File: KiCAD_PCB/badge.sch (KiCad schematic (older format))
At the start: 78 parts, among them Q1 BC847, Q2 BC847, Q3 BC847, U1 switch, U2 LM1117-3.3, U3 button, U4 digijoy, U5 button, U6 wrover, U7 2jumpers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

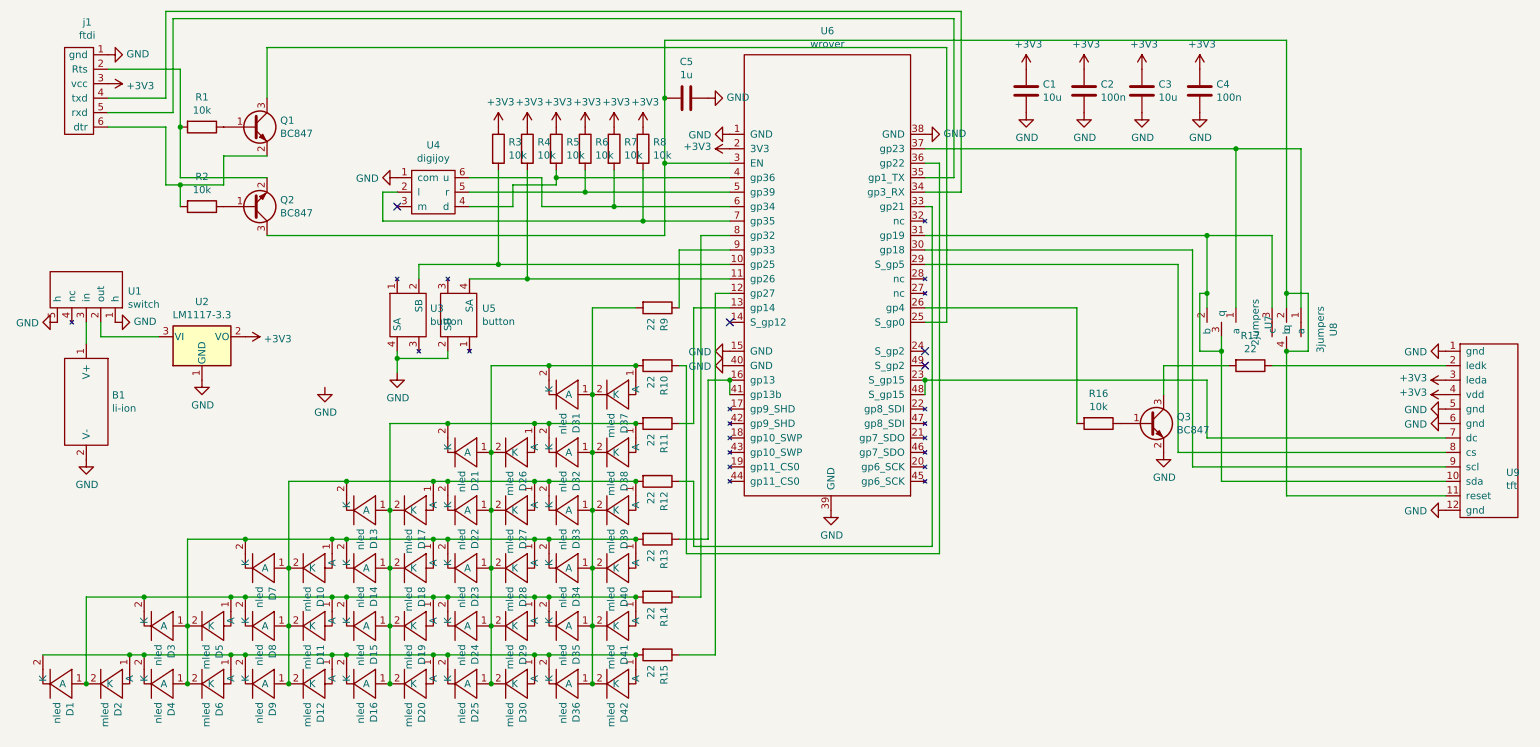
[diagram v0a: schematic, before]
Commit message: deleted two-transistor helper circuit on gp0/reset that was causing trouble when not connected to an ftdi module same circuit now included in programmer
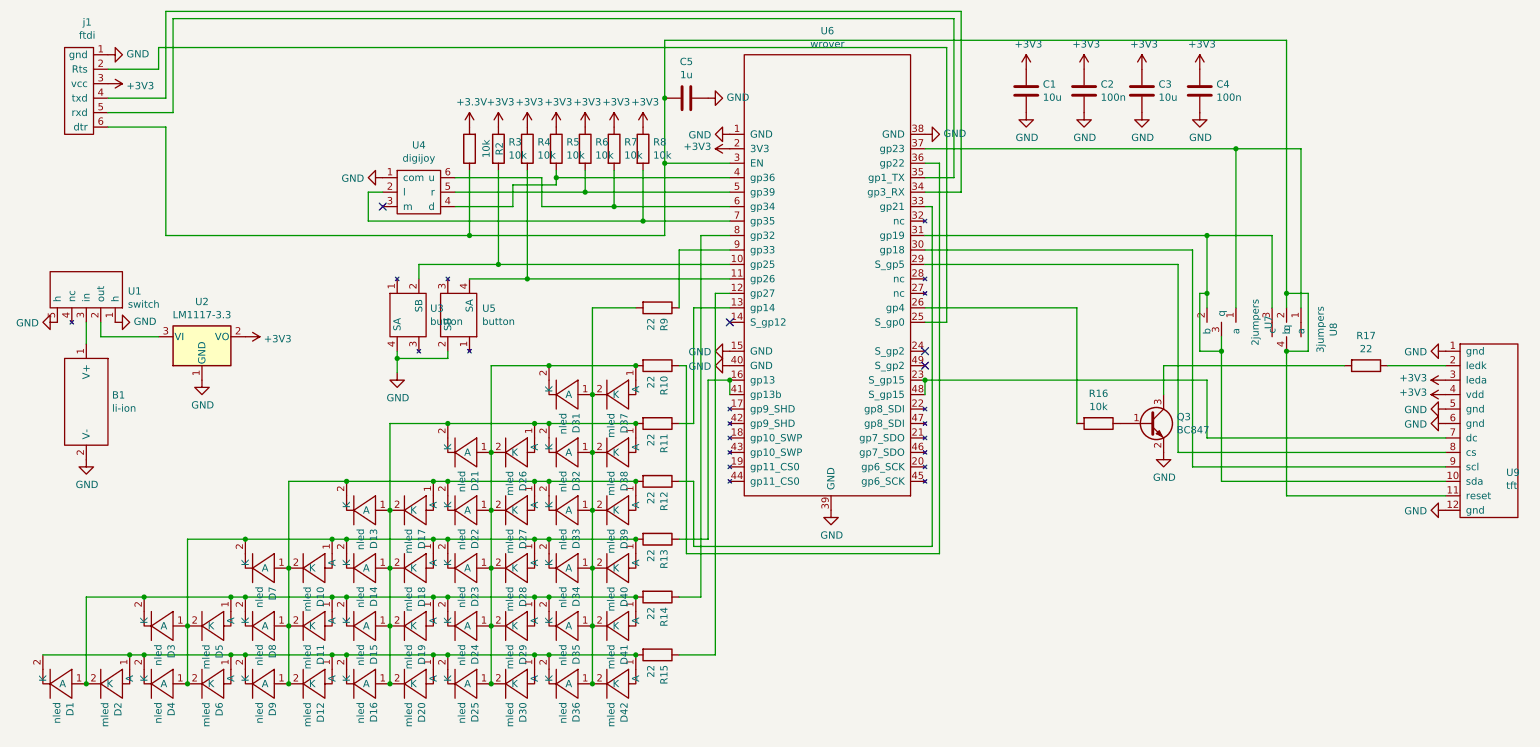
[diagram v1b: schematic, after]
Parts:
- removed Q1, Q2: BC847, Package_TO_SOT_SMD:SOT-23, symbol Transistor_BJT:BC847
- removed R1: 10k, LED_SMD:LED_1206_3216Metric_Pad1.42x1.75mm_HandSolder, symbol Device:R
- U8: footprint badge:2jumpers -> badge:3jumpers
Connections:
- net +3V3: now also R2.2
- net at U6.25 (S_gp0): now also j1.2 (Rts)
- net at C5.2, U6.3 (EN), U8.2 (b)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: now also R2.1, j1.6 (dtr)
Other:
- moved on the sheet: R17, R2, U4
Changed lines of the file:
@@
 EESchema Schematic File Version 4
-LIBS:badge-cache
 EELAYER 26 0
 EELAYER END
@@
 L badge:digijoy U4
 U 1 1 5F04E97E
-P 3300 4000
-F 0 "U4" H 3300 4325 50  0000 C CNN
-F 1 "digijoy" H 3300 4234 50  0000 C CNN
-F 2 "badge:digijoy" H 3300 4000 50  0001 C CNN
-F 3 "" H 3300 4000 50  0001 C CNN
-	1    3300 4000
-	1    0    0    -1
-$EndComp
-Wire Wire Line
-	3050 4000 2950 4000
-Wire Wire Line
-	2950 4000 2950 4200
-Wire Wire Line
-	2950 4200 4750 4200
+P 3200 4000
+F 0 "U4" H 3200 4325 50  0000 C CNN
+F 1 "digijoy" H 3200 4234 50  0000 C CNN
+F 2 "badge:digijoy" H 3200 4000 50  0001 C CNN
+F 3 "" H 3200 4000 50  0001 C CNN
+	1    3200 4000
+	1    0    0    -1
+$EndComp
+Wire Wire Line
+	2950 4000 2850 4000
+Wire Wire Line
+	2850 4000 2850 4200
 $Comp
 L power:GND #PWR0106
 U 1 1 5F0584DB
-P 3050 3900
-F 0 "#PWR0106" H 3050 3650 50  0001 C CNN
-F 1 "GND" V 3055 3772 50  0000 R CNN
-F 2 "" H 3050 3900 50  0001 C CNN
-F 3 "" H 3050 3900 50  0001 C CNN
-	1    3050 3900
+P 2950 3900
+F 0 "#PWR0106" H 2950 3650 50  0001 C CNN
+F 1 "GND" V 2955 3772 50  0000 R CNN
+F 2 "" H 2950 3900 50  0001 C CNN
+F 3 "" H 2950 3900 50  0001 C CNN
+	1    2950 3900
 	0    1    1    0
 $EndComp
@@
 	4750 4200 4750 3850
 $Comp
-L Transistor_BJT:BC847 Q1
-U 1 1 5F084BB7
-P 2050 3550
-F 0 "Q1" H 2241 3596 50  0000 L CNN
-F 1 "BC847" H 2241 3505 50  0000 L CNN
-F 2 "Package_TO_SOT_SMD:SOT-23" H 2250 3475 50  0001 L CIN
-F 3 "http://www.infineon.com/dgdl/Infineon-BC847SERIES_BC848SERIES_BC849SERIES_BC850SERIES-DS-v01_01-en.pdf?fileId=db3a304314dca389011541d4630a1657" H 2050 3550 50  0001 L CNN
-	1    2050 3550
-	1    0    0    -1
-$EndComp
-$Comp
-L Transistor_BJT:BC847 Q2
-U 1 1 5F084EBC
-P 2050 4100
-F 0 "Q2" H 2241 4054 50  0000 L CNN
-F 1 "BC847" H 2241 4145 50  0000 L CNN
-F 2 "Package_TO_SOT_SMD:SOT-23" H 2250 4025 50  0001 L CIN
-F 3 "http://www.infineon.com/dgdl/Infineon-BC847SERIES_BC848SERIES_BC849SERIES_BC850SERIES-DS-v01_01-en.pdf?fileId=db3a304314dca389011541d4630a1657" H 2050 4100 50  0001 L CNN
-	1    2050 4100
-	1    0    0    1
-$EndComp
-$Comp
 L Transistor_BJT:BC847 Q3
 U 1 1 5F08505C
@@
 $EndComp
 $Comp
-L Device:R R1
-U 1 1 5F085226
-P 1700 3550
-F 0 "R1" V 1493 3550 50  0000 C CNN
-F 1 "10k" V 1584 3550 50  0000 C CNN
-F 2 "LED_SMD:LED_1206_3216Metric_Pad1.42x1.75mm_HandSolder" V 1630 3550 50  0001 C CNN
-F 3 "~" H 1700 3550 50  0001 C CNN
-	1    1700 3550
-	0    1    1    0
-$EndComp
-$Comp
 L Device:R R2
 U 1 1 5F0853DE
-P 1700 4100
-F 0 "R2" V 1493 4100 50  0000 C CNN
-F 1 "10k" V 1584 4100 50  0000 C CNN
-F 2 "LED_SMD:LED_1206_3216Metric_Pad1.42x1.75mm_HandSolder" V 1630 4100 50  0001 C CNN
-F 3 "~" H 1700 4100 50  0001 C CNN
-	1    1700 4100
-	0    1    1    0
-$EndComp
-Wire Wire Line
-	1550 3550 1550 3900
-Wire Wire Line
-	1550 3900 2150 3900
-Wire Wire Line
-	2150 3750 1850 3750
-Wire Wire Line
-	1850 3750 1850 3950
-Wire Wire Line
-	1850 3950 1550 3950
-Wire Wire Line
-	1550 3950 1550 4100
-Wire Wire Line
-	2150 4300 4900 4300
+P 3550 3700
+F 0 "R2" V 3343 3700 50  0000 C CNN
+F 1 "10k" V 3434 3700 50  0000 C CNN
+F 2 "LED_SMD:LED_1206_3216Metric_Pad1.42x1.75mm_HandSolder" V 3480 3700 50  0001 C CNN
+F 3 "~" H 3550 3700 50  0001 C CNN
+	1    3550 3700
+	-1   0    0    1
+$EndComp
+Wire Wire Line
+	3550 4300 4900 4300
 Wire Wire Line
 	4900 4300 4900 3800
@@
 	4900 3800 5350 3800
 Wire Wire Line
-	2150 3350 2150 3000
-Wire Wire Line
-	2150 3000 6850 3000
+	1400 3000 6850 3000
 Wire Wire Line
 	6850 3000 6850 4900
@@
 	3200 4500 3200 4600
 $Comp
-L power:GND #PWR0115
-U 1 1 5F0A70A6
-P 2550 5350
-F 0 "#PWR0115" H 2550 5100 50  0001 C CNN
-F 1 "GND" H 2555 5177 50  0000 C CNN
-F 2 "" H 2550 5350 50  0001 C CNN
-F 3 "" H 2550 5350 50  0001 C CNN
-	1    2550 5350
-	1    0    0    -1
-$EndComp
-$Comp
 L power:GND #PWR0116
 U 1 1 5F0A718E
@@
 	1    0    0    -1
 $EndComp
-Connection ~ 4750 4200
 Connection ~ 4350 4000
 Wire Wire Line
@@
 	3750 4500 5350 4500
 Wire Wire Line
-	4350 4000 3550 4000
-Wire Wire Line
 	4150 3900 5350 3900
 Wire Wire Line
@@
 F 0 "U8" H 9150 5325 50  0000 C CNN
 F 1 "3jumpers" H 9150 5234 50  0000 C CNN
-F 2 "badge:2jumpers" H 9200 5000 50  0001 C CNN
+F 2 "badge:3jumpers" H 9200 5000 50  0001 C CNN
 F 3 "" H 9200 5000 50  0001 C CNN
 	1    9200 5000
@@
 L Device:R R17
 U 1 1 5F1ADE3C
-P 8950 5200
-F 0 "R17" V 8743 5200 50  0000 C CNN
-F 1 "22" V 8834 5200 50  0000 C CNN
-F 2 "LED_SMD:LED_1206_3216Metric_Pad1.42x1.75mm_HandSolder" V 8880 5200 50  0001 C CNN
-F 3 "~" H 8950 5200 50  0001 C CNN
-	1    8950 5200
+P 9750 5200
+F 0 "R17" V 9543 5200 50  0000 C CNN
+F 1 "22" V 9634 5200 50  0000 C CNN
+F 2 "LED_SMD:LED_1206_3216Metric_Pad1.42x1.75mm_HandSolder" V 9680 5200 50  0001 C CNN
+F 3 "~" H 9750 5200 50  0001 C CNN
+	1    9750 5200
 	0    1    1    0
 $EndComp
@@
 	8350 5400 8350 5200
 Wire Wire Line
-	8350 5200 8800 5200
-Wire Wire Line
-	9100 5200 10300 5200
+	8350 5200 9600 5200
+Wire Wire Line
+	9900 5200 10300 5200
 Wire Wire Line
 	6700 4800 7750 4800
@@
 $EndComp
 Wire Wire Line
-	1050 3150 1550 3150
-Wire Wire Line
-	1550 3150 1550 3550
-Connection ~ 1550 3550
+	1050 3150 1400 3150
 Wire Wire Line
 	1050 3550 1450 3550
-Wire Wire Line
-	1450 3550 1450 3950
-Wire Wire Line
-	1450 3950 1550 3950
-Connection ~ 1550 3950
 $Comp
 L power:GND #PWR0131
@@
 NoConn ~ 6700 5100
 NoConn ~ 6700 5200
-NoConn ~ 3050 4100
+NoConn ~ 2950 4100
 $Comp
 L power:GND #PWR0137
@@
 Wire Wire Line
 	4050 4100 4050 3900
-Wire Wire Line
-	4050 3900 3550 3900
 Connection ~ 4550 4100
-Wire Wire Line
-	3550 4100 3850 4100
 Wire Wire Line
 	3850 4100 3850 3950
@@
 	9200 4700 9200 4800
 Connection ~ 9200 5100
+Wire Wire Line
+	1400 3150 1400 3000
+Wire Wire Line
+	3450 3900 4050 3900
+Wire Wire Line
+	3450 4000 4350 4000
+Wire Wire Line
+	3450 4100 3850 4100
+Wire Wire Line
+	2850 4200 4750 4200
+Connection ~ 4750 4200
+Wire Wire Line
+	3550 3850 3550 4300
+$Comp
+L power:+3.3V #PWR0115
+U 1 1 5F49C3E8
+P 3550 3550
+F 0 "#PWR0115" H 3550 3400 50  0001 C CNN
+F 1 "+3.3V" H 3565 3723 50  0000 C CNN
+F 2 "" H 3550 3550 50  0001 C CNN
+F 3 "" H 3550 3550 50  0001 C CNN
+	1    3550 3550
+	1    0    0    -1
+$EndComp
+Wire Wire Line
+	3550 4300 1450 4300
+Wire Wire Line
+	1450 4300 1450 3550
+Connection ~ 3550 4300
 $EndSCHEMATC
